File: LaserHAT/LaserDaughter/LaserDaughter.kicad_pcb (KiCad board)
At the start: 2 copper layers, 26.5 x 23.5 mm, 29 parts, among them J1 HAT_J8, J2 Conn_02x02_Counter_Clockwise, J3 HAT_J9, J4 PD_K-LASER_V (solder jumper), J5 RED_SHUNT, Q1 SI3134KDWA-TP, Q2 NDT3055L, SW5 PCM12SMTR, U2 MT3608, U3 TLV2371DBV

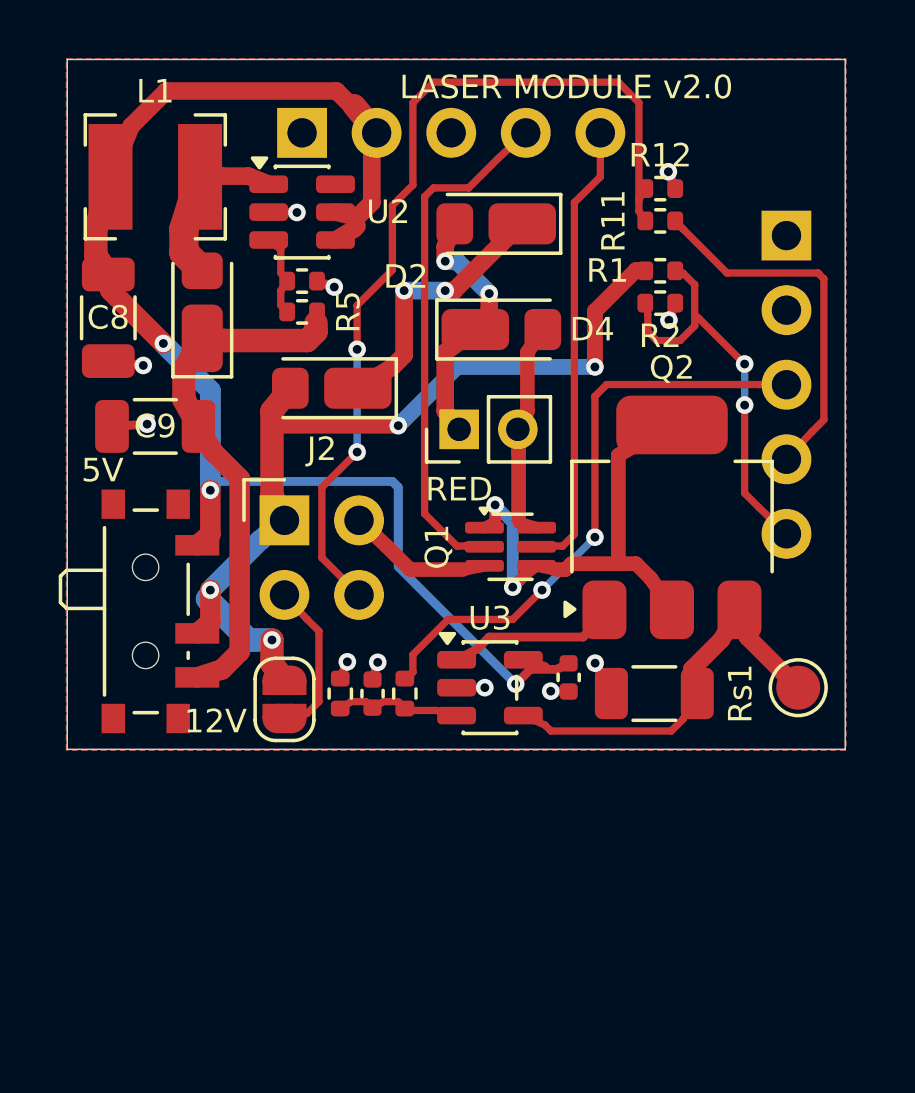
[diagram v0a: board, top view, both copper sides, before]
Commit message: Updated layout of laser daughter PCB
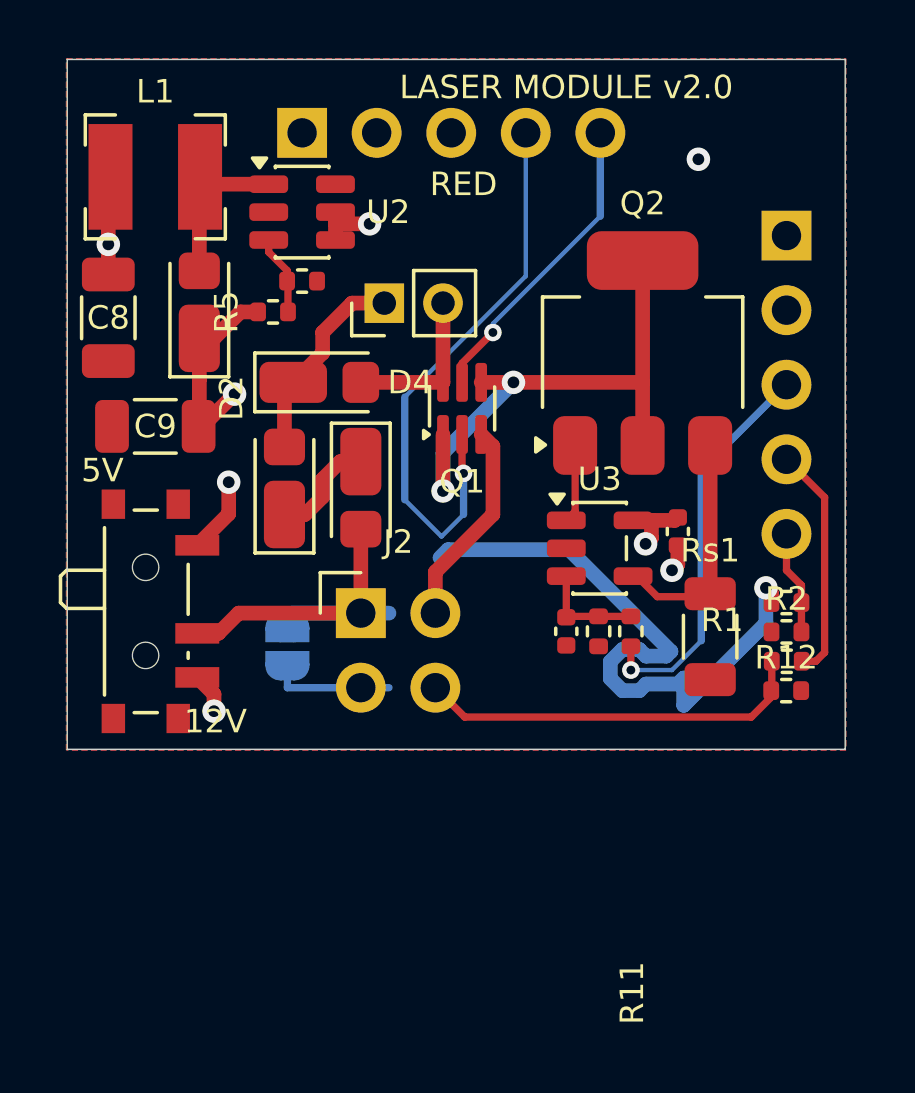
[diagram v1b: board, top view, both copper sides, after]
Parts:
- removed TP1: TestPoint, TestPoint:TestPoint_Pad_D1.5mm
- J4: moved to B.Cu
- moved R12 17.6 mm to (125.5, 97.5)
- moved R11 15.6 mm to (125.5, 96.5)
- moved R1 12.1 mm to (125.5, 94.5)
- moved R2 12.0 mm to (125.5, 95.5), turned to 180 degrees
- moved D2 11.5 mm to (108.4, 90.6), turned to 90 degrees
- moved R4 9.05 mm to (119.1, 95.5), turned to -90 degrees
- moved R3 7.99 mm to (120.2, 95.5), turned to 90 degrees
- moved C11 6.93 mm to (118.0, 95.5), turned to -90 degrees
- moved D4 6.46 mm to (109.6, 87.0)
- moved C12 6.21 mm to (121.8, 92.1)
- moved U3 6.04 mm to (119.1, 92.7)
- moved Q2 5.69 mm to (120.6, 86.0)
- moved J5 5.00 mm to (111.8, 84.3)
- moved Q1 4.99 mm to (114.5, 87.9), turned to 90 degrees
- moved J2 4.09 mm to (111.0, 94.9)
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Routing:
- net Net-(J2-PD_Anode): track 31.4 -> 13.3 mm, vias 2 -> 0
- net DB_ADC_B: track 13.8 -> 3.55 mm, vias 2 -> 0
- net GND: track 9.20 -> 0.92 mm, vias 11 -> 2
- net DB_DAC: track 20.3 -> 13.5 mm, vias 2 -> 1
- net /IDrive: track 13.6 -> 8.01 mm
- net LASER_V: track 30.0 -> 35.5 mm, vias 4 -> 1
- net /DUMMY_TOP: track 9.10 -> 3.70 mm, vias 2 -> 0
- net DB_PWM_A: track 15.5 -> 10.5 mm, vias 0 -> 1
- net DB_ADC_A: track 12.5 -> 8.02 mm
- net +12V: track 17.9 -> 21.1 mm, vias 0 -> 2
- net Net-(Q2-G): track 5.75 -> 2.67 mm
- net +5V: track 48.9 -> 46.7 mm, vias 3 -> 4
- net /LaserDrive: track 16.2 -> 18.4 mm
- net DB_PWM_B: track 17.6 -> 19.8 mm, vias 0 -> 1
- net Net-(J2-LD_Cathode): track 4.96 -> 7.06 mm
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- added copper zone on In1.Cu, net GND
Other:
- copper layers 2 -> 4

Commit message: Updated laser daughter PCB design with higher current PWM switch
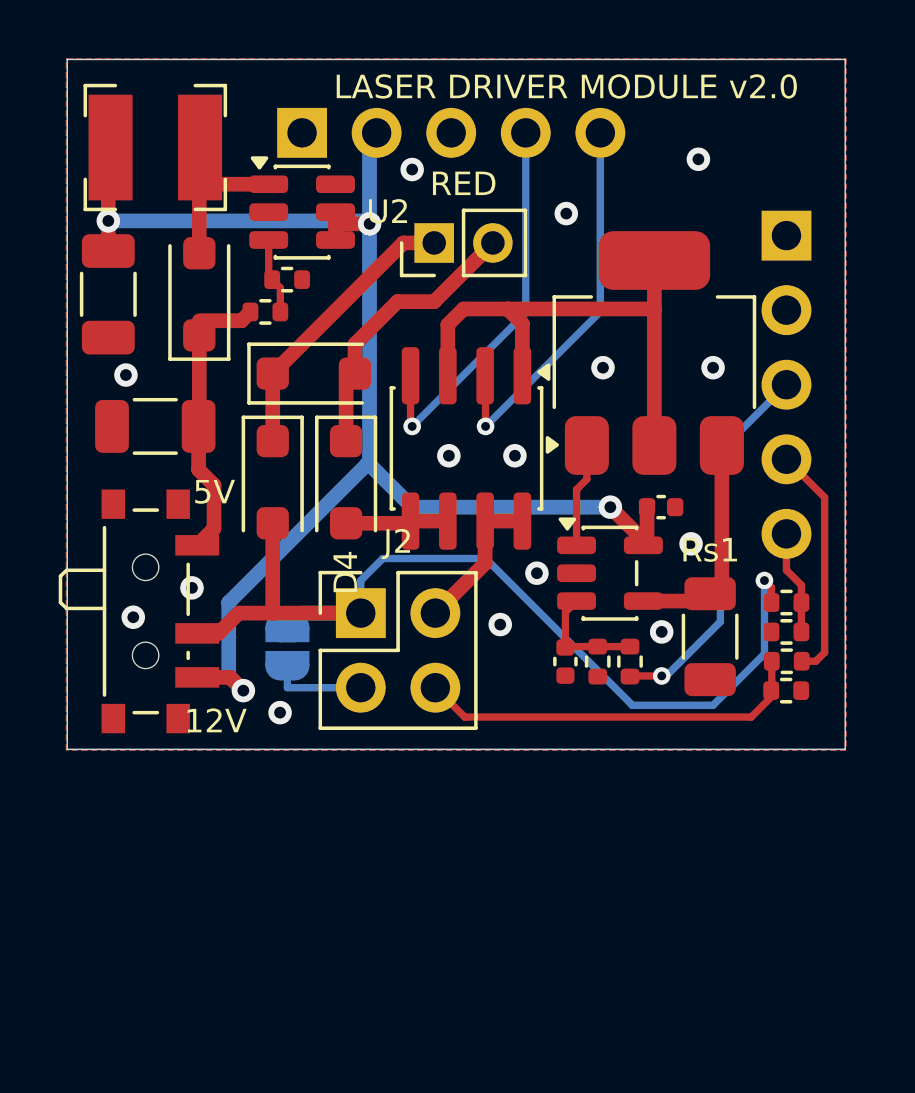
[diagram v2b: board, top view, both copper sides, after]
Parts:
- D2: value 2.4V 1W (KDZVTR2.4B) -> 2.7V 1W (KDZVTR2.7B)
- D4: value 2.7V 1W (KDZVTR2.7B) -> 2.4V 1W (KDZVTR2.4B)
- Q1: value SI3134KDWA-TP -> AO9926B; footprint Package_TO_SOT_SMD:SOT-363_SC-70-6 -> Package_SO:SOIC-8_3.9x4.9mm_P1.27mm
- moved D2 4.03 mm to (109.4, 86.7), turned to 0 degrees
- moved D4 3.52 mm to (110.5, 90.4), turned to -90 degrees
- moved D3 3.01 mm to (108.0, 90.4)
- moved J5 2.66 mm to (113.5, 82.2)
- moved Q1 1.37 mm to (114.6, 89.2), turned to -90 degrees
- moved C11 1.03 mm to (118.0, 96.5)
- moved R3 1.03 mm to (120.2, 96.5)
- moved R4 1.03 mm to (119.1, 96.5)
- moved C12 1.01 mm to (121.2, 91.2), turned to 0 degrees
- moved L1 1.00 mm to (104.0, 79.0)
- moved U3 0.92 mm to (119.5, 93.5)
- moved C8 0.80 mm to (102.4, 84.0)
- moved D1 0.60 mm to (105.5, 84.0)
- moved R6 0.51 mm to (108.5, 83.5)
- moved Q2 0.40 mm to (121.0, 86.0)
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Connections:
- J5 pad 1: /DUMMY_MID -> /DUMMY_TOP
- J5 pad 2: /DUMMY_BOT -> /DUMMY_MID
- Q1 pad 2: DB_PWM_B -> DB_PWM_A
- Q1 pad 3: Net-(J2-LD_Cathode) -> /LaserDrive
- Q1 pad 4: /LaserDrive -> DB_PWM_B
- Q1 pad 5: DB_PWM_A -> /DUMMY_BOT
- SW5 pad 1: +5V -> +12V
- SW5 pad 3: +12V -> +5V
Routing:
- net +12V: track 21.1 -> 9.44 mm, vias 2 -> 0
- net DB_PWM_B: track 19.8 -> 13.4 mm
- net /DUMMY_TOP: track 3.70 -> 9.64 mm
- net DB_PWM_A: track 10.5 -> 13.3 mm
- net /DUMMY_MID: track 6.95 -> 9.55 mm
- net LASER_V: track 35.5 -> 32.9 mm
- net /DUMMY_BOT: track 5.50 -> 3.50 mm
- net Net-(J2-LD_Cathode): track 7.06 -> 5.11 mm
- net +5V: track 46.7 -> 48.2 mm
- net Net-(J2-PD_Cathode): track 4.21 -> 3.25 mm
- net GND: track 0.92 -> 0.00 mm, vias 2 -> 15
- net Net-(Q2-G): track 2.67 -> 3.54 mm
- net /IDrive: track 8.01 -> 7.24 mm
- net DB_DAC: track 13.5 -> 12.8 mm
- net /LaserDrive: track 18.4 -> 17.8 mm, vias 2 -> 0
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- removed copper zone on In1.Cu, net GND
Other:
- copper layers 4 -> 2
- board text added: "KemereLab.org (c)2026.10"
- board text added: "LASER DRIVER MODULE v2.0"
- board text added: "sdg"
- board text removed: "HAT J8"
- board text removed: "HAT J9"
- board text removed: "LASER MODULE v2.0"
